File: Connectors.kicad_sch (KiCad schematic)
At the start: 1 part, among them J3 Conn_02x17_Odd_Even

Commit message: wip
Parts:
- J3: footprint Connector_IDC:IDC-Header_2x17_P2.54mm_Horizontal -> Connector_IDC:IDC-Header_2x17_P2.54mm_Vertical
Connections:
- net EM_STOP renamed Disable_Drive
- net Encoder_A: no longer names the net of J3.31 (Pin_31)
- net Encoder_B: no longer names the net of J3.33 (Pin_33)
- net Encoder_C: no longer names the net of J3.34 (Pin_34)
- no-connect marks 2 -> 6

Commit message: 90% schematic first layout
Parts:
- added J7: Screw_Terminal_01x16, TerminalBlock:TerminalBlock_Xinya_XY308-2.54-16P_1x16_P2.54mm_Horizontal, symbol Connector:Screw_Terminal_01x16
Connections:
- net GNDD: now also J7.2 (Pin_2), J7.4 (Pin_4), J7.6 (Pin_6), J7.8 (Pin_8)
- new net +24V: J7.1 (Pin_1)
- new net ERROR_LED+: J7.11 (Pin_11)
- new net ERROR_LED-: J7.12 (Pin_12)
- new net ESTOP: J7.7 (Pin_7)
- new net ESTOP_LED+: J7.13 (Pin_13)
- new net ESTOP_LED-: J7.14 (Pin_14)
- new net Error_Fixed: J7.5 (Pin_5)
- new net RUN_LED+: J7.9 (Pin_9)
- new net RUN_LED-: J7.10 (Pin_10)
- new net RUN/STOP: J7.3 (Pin_3)
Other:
- moved on the sheet: J3

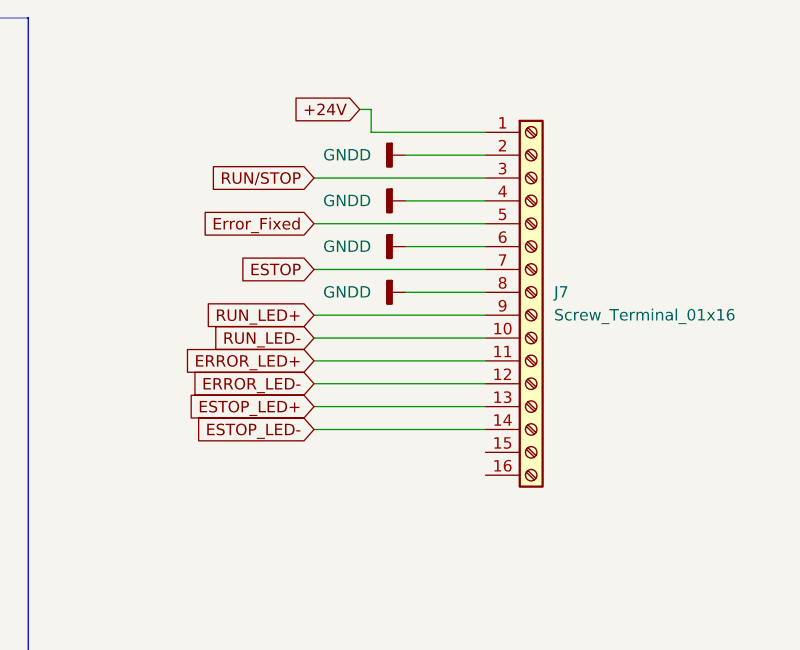
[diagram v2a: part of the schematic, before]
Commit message: Addition of testpoints
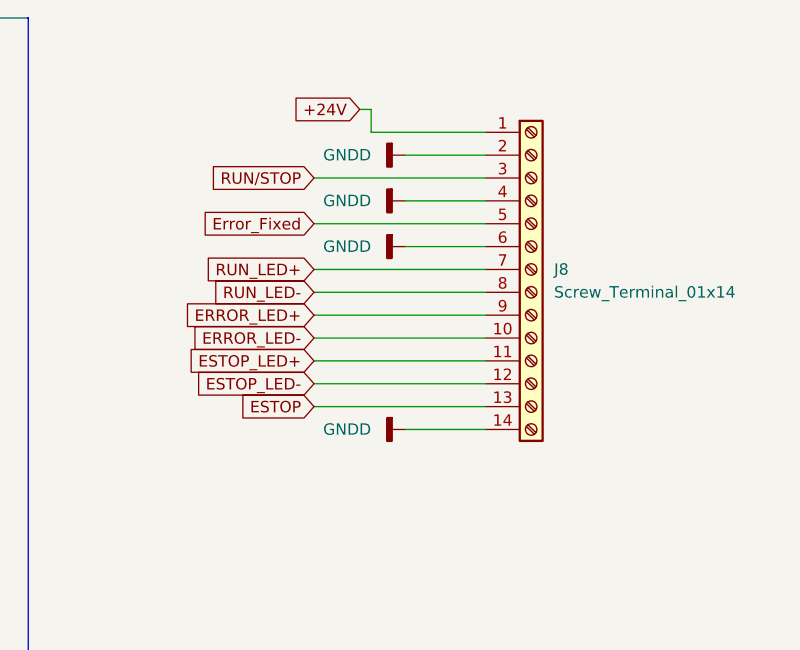
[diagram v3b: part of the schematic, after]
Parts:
- removed J7: Screw_Terminal_01x16, TerminalBlock:TerminalBlock_Xinya_XY308-2.54-16P_1x16_P2.54mm_Horizontal, symbol Connector:Screw_Terminal_01x16
- added J8: Screw_Terminal_01x14, TerminalBlock:TerminalBlock_Xinya_XY308-2.54-14P_1x14_P2.54mm_Horizontal, symbol Connector:Screw_Terminal_01x14
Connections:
- net +24V: now also J8.1 (Pin_1)
- net ERROR_LED+: now also J8.9 (Pin_9)
- net ERROR_LED-: now also J8.10 (Pin_10)
- net ESTOP: now also J8.13 (Pin_13)
- net ESTOP_LED+: now also J8.11 (Pin_11)
- net ESTOP_LED-: now also J8.12 (Pin_12)
- net Error_Fixed: now also J8.5 (Pin_5)
- net GNDD: now also J8.14 (Pin_14), J8.2 (Pin_2), J8.4 (Pin_4), J8.6 (Pin_6)
- net RUN_LED+: now also J8.7 (Pin_7)
- net RUN_LED-: now also J8.8 (Pin_8)
- net RUN/STOP: now also J8.3 (Pin_3)
